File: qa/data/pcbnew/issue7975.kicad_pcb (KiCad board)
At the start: 2 copper layers, 73.7 x 55.3 mm, 2 parts, among them U101 4021, U102 4021

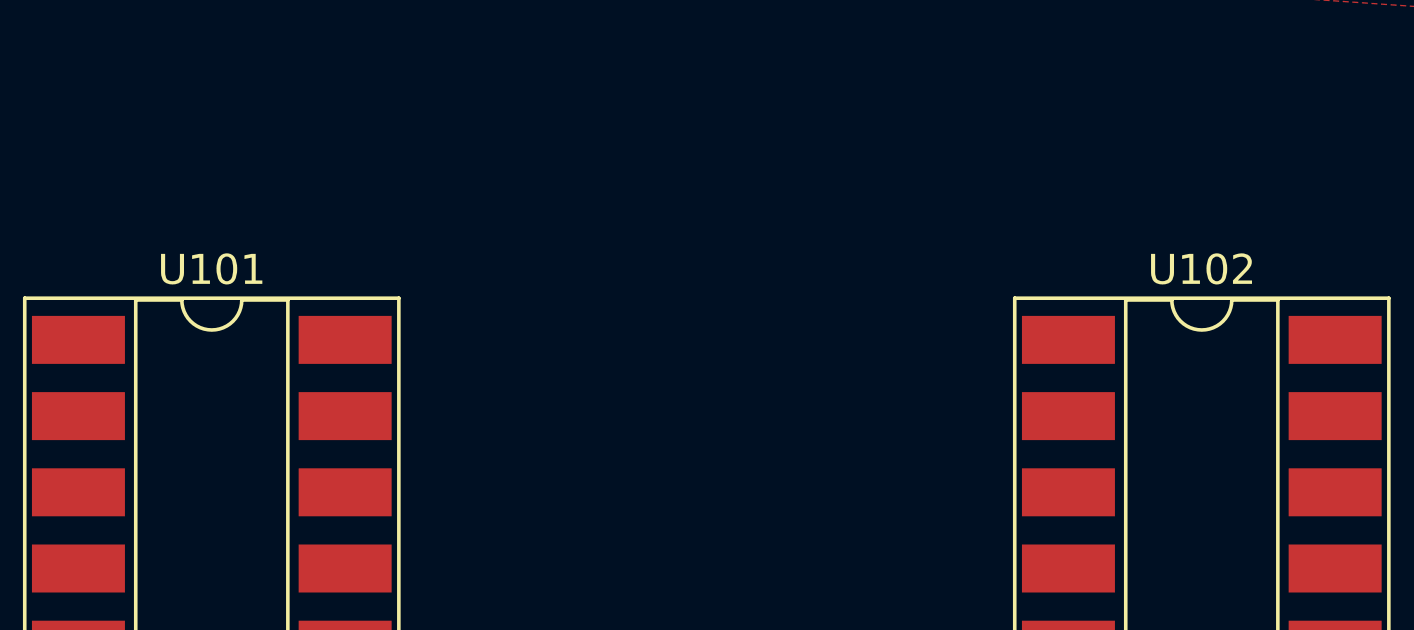
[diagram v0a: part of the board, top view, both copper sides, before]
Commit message: Update qa tests to use new zone fill algo
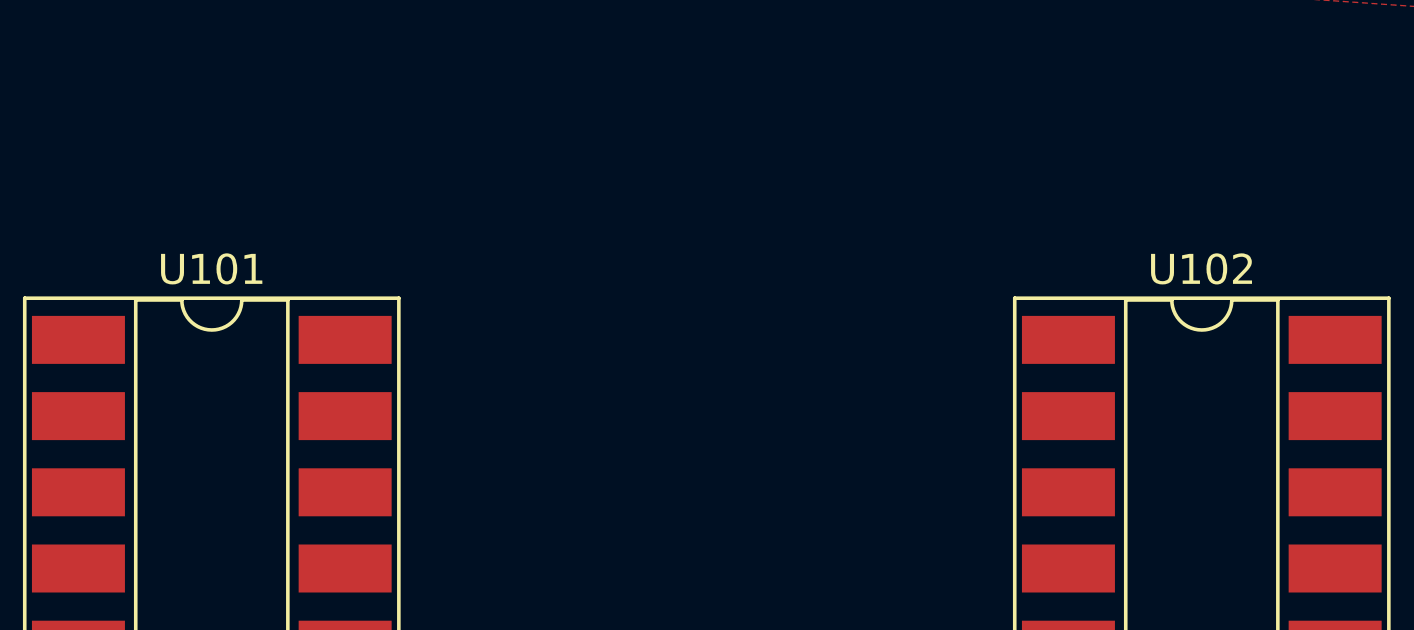
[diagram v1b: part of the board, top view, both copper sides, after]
